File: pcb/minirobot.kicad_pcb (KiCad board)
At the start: 2 copper layers, 50 x 50 mm, 68 parts, among them P1 FEELERLEFT, P2 SERVO, P3 BATTERY, P4 FEELERRIGHT, P5 SERVO, U1 LINELEFTOUT, U10 WHEELRIGHT, U11 STM32SWDUART, U12 STM32F411RET6, U2 WHEELLEFT, U3 LINELEFTIN, U4 TCS3472, U5 RN4020, U6 ST-LIS3MDL, U7 LINERIGHTIN, U8 DIODES-AP3211, U9 LINERIGHTOUT

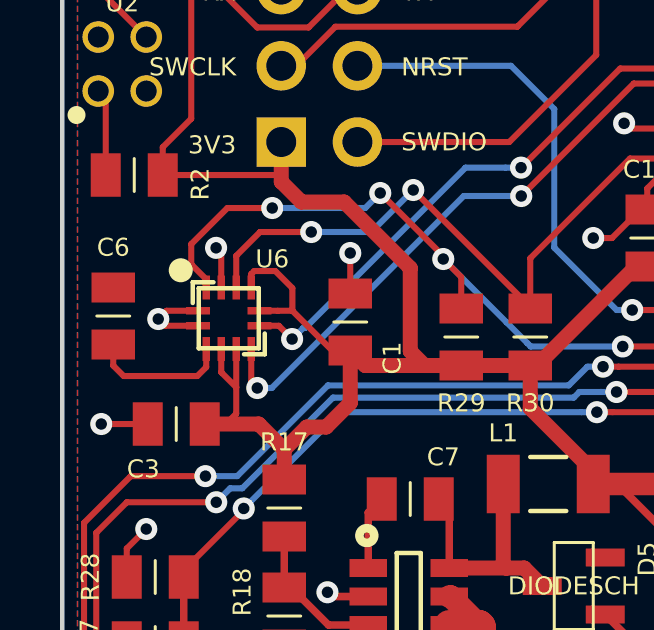
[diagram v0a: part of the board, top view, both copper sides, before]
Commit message: add compass x/y markings on silk
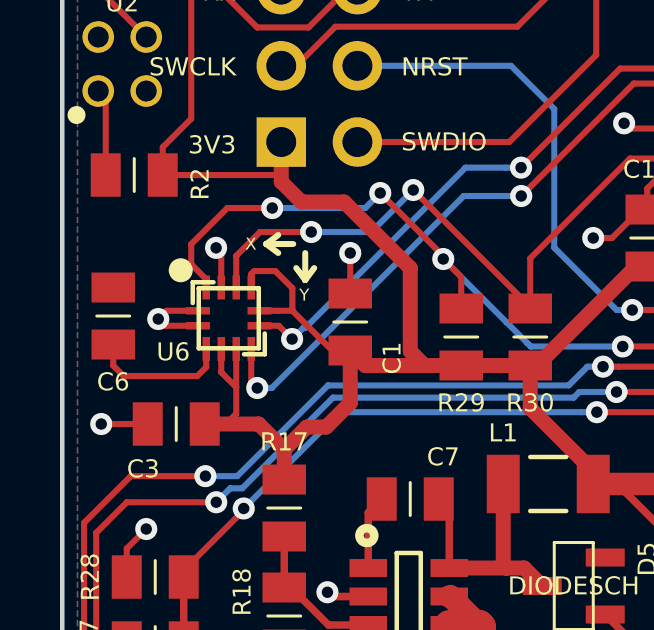
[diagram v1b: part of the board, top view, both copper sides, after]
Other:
- board text added: "X"
- board text added: "Y"
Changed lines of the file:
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@@
     (area 97.725371 38.511799 180.978201 129.078201)
     (thickness 1.6)
-    (drawings 39)
+    (drawings 47)
     (tracks 826)
     (zones 0)
@@
   (module kicadlib:CAPC2012X100N (layer F.Cu)
     (at 101.7 78.6 90)
-    (fp_text reference C6 (at 2.286 0 180) (layer F.SilkS)
+    (fp_text reference C6 (at -2.2 0 180) (layer F.SilkS)
       (effects (font (size 0.6 0.6) (thickness 0.1)))
     )
@@
   (module kicadlib:LGA12S50P4X4_192X192X100 (layer F.Cu)
     (at 105.55 78.675)
-    (fp_text reference U6 (at 1.45 -1.975) (layer F.SilkS)
+    (fp_text reference U6 (at -1.85 1.125) (layer F.SilkS)
       (effects (font (size 0.6 0.6) (thickness 0.1)))
     )
@@
       (net 2 GNDPWR))
   )
+  (gr_text Y (at 107.9 77.9) (layer F.SilkS)
+    (effects (font (size 0.4 0.4) (thickness 0.08)) (justify left))
+  )
+  (gr_line (start 108.1 77.4) (end 107.8 77) (layer F.SilkS) (width 0.2))
+  (gr_line (start 108.1 77.4) (end 108.4 77) (layer F.SilkS) (width 0.2))
+  (gr_line (start 108.1 76.5) (end 108.1 77.4) (layer F.SilkS) (width 0.2))
+  (gr_text X (at 106.1 76.2) (layer F.SilkS)
+    (effects (font (size 0.4 0.4) (thickness 0.08)) (justify left))
+  )
+  (gr_line (start 106.8 76.2) (end 107.2 76.5) (layer F.SilkS) (width 0.2))
+  (gr_line (start 106.8 76.2) (end 107.2 75.9) (layer F.SilkS) (width 0.2))
+  (gr_line (start 107.7 76.2) (end 106.8 76.2) (layer F.SilkS) (width 0.2))
   (gr_text ON (at 118.4 93.4) (layer F.SilkS)
     (effects (font (size 0.6 0.6) (thickness 0.1)) (justify left))

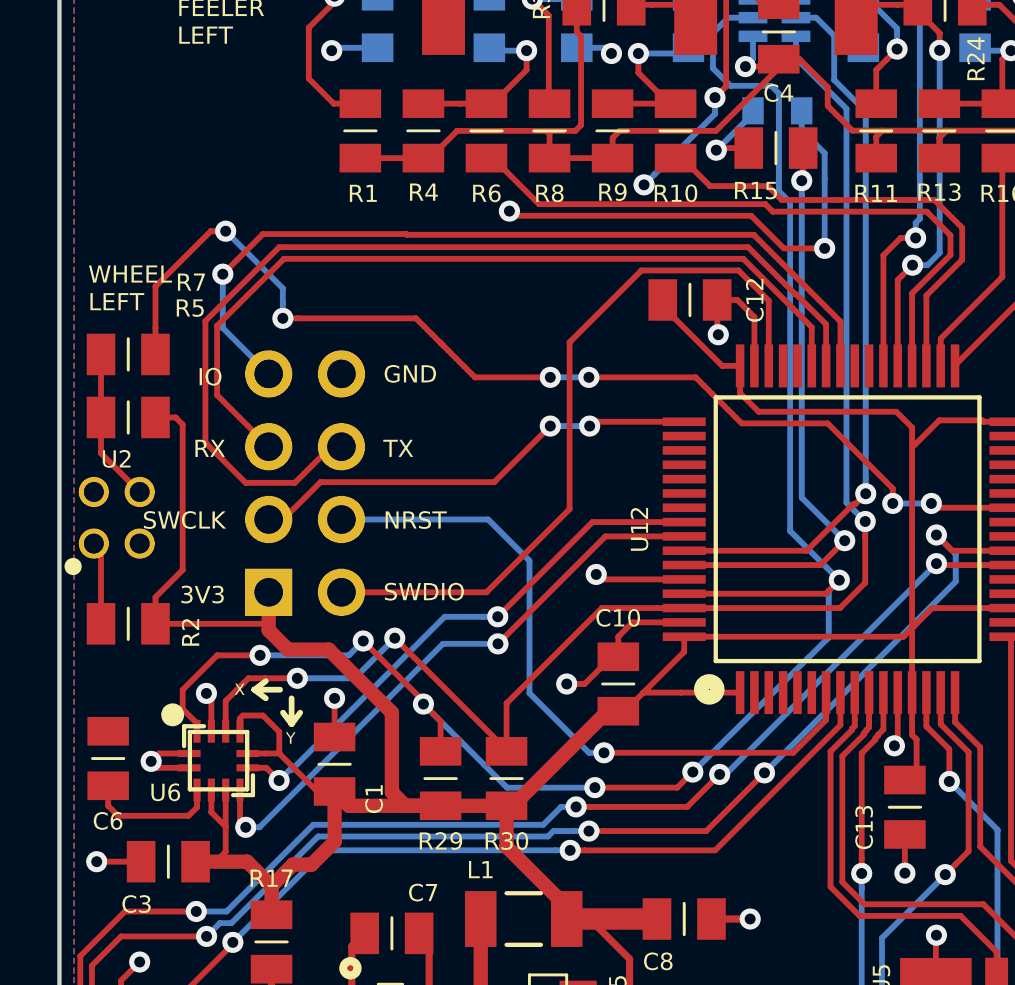
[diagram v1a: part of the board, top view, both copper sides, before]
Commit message: move SWD/Debug connector to make it easier for compass rework
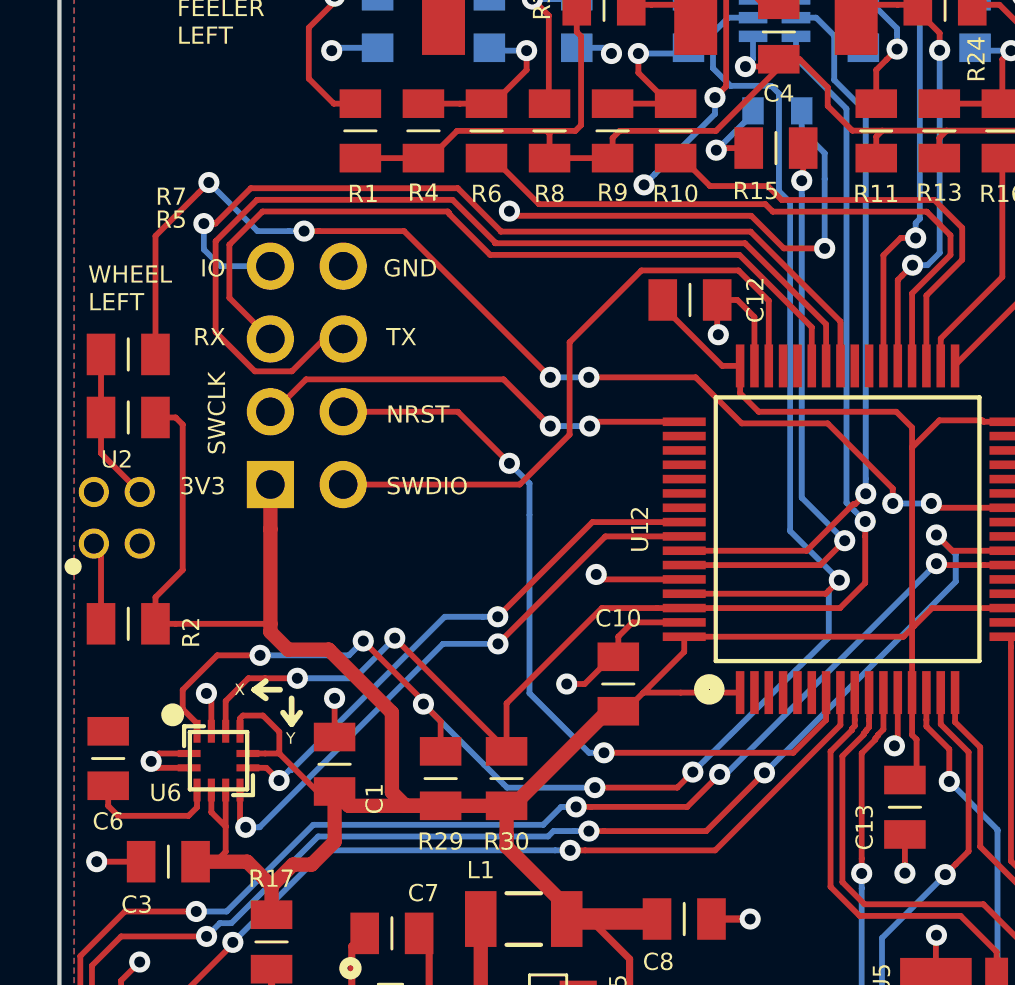
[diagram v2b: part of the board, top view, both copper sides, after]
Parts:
- moved U11 3.76 mm to (107.4, 69.0)
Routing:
- net /SWDIO: track 25.7 -> 22.5 mm
- net /NRST: track 24.4 -> 27.5 mm, vias 1 -> 2
- net +3.3V: track 249.6 -> 252.3 mm
- net /Sensors/WHEELLEFT: track 38.1 -> 39.8 mm
- net /DEBUGTX: track 35.4 -> 33.8 mm
- net /DEBUGRX: track 29.0 -> 27.7 mm
- net /DEBUGGPIO: track 29.1 -> 29.7 mm
